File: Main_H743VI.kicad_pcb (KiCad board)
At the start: 4 copper layers, 150 x 100 mm, 71 parts, among them J1 ST-LINK, J10 AS7265X, J11 TFT_LCD2, J12 SERVO1, J13 USER_GPIO, J14 TFT_LCD, J15 SERVO2, J16 FAN, J17 ADC_IN, J2 USB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

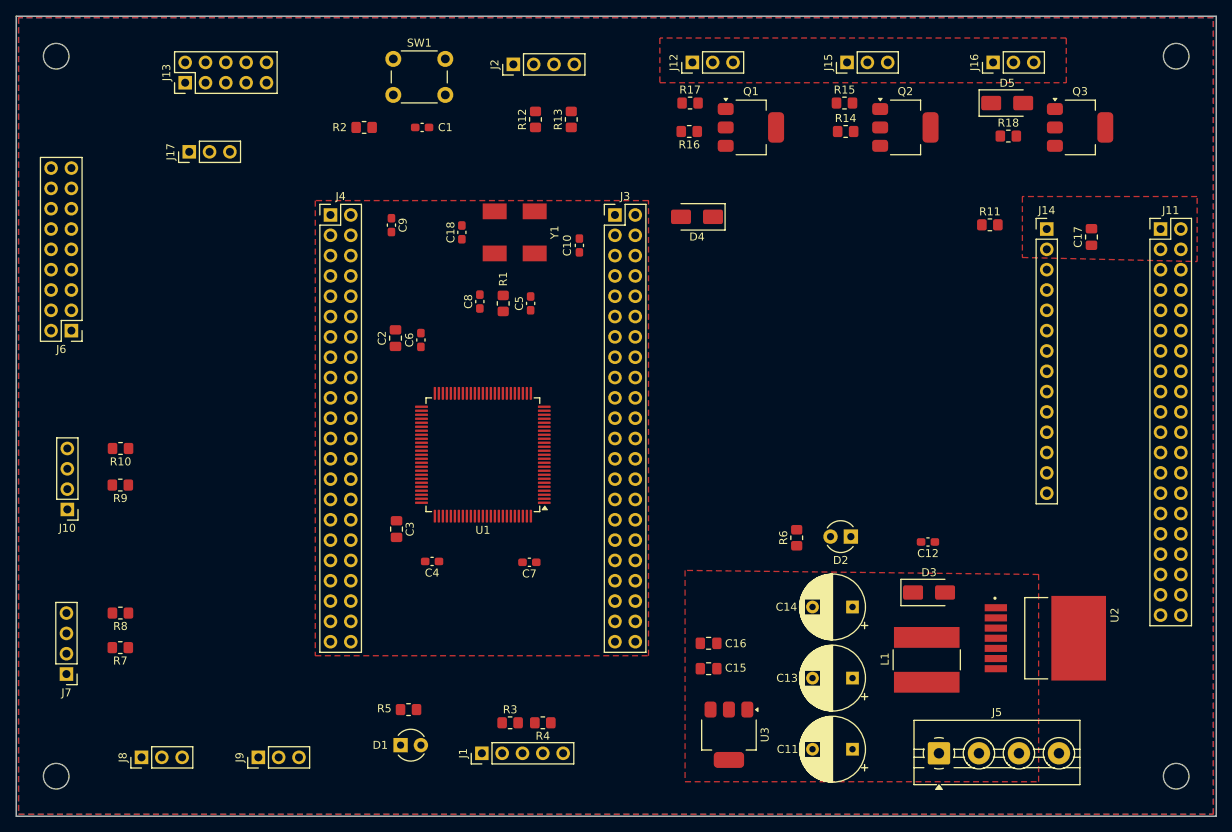
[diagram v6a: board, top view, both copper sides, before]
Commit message: flipped camera connector
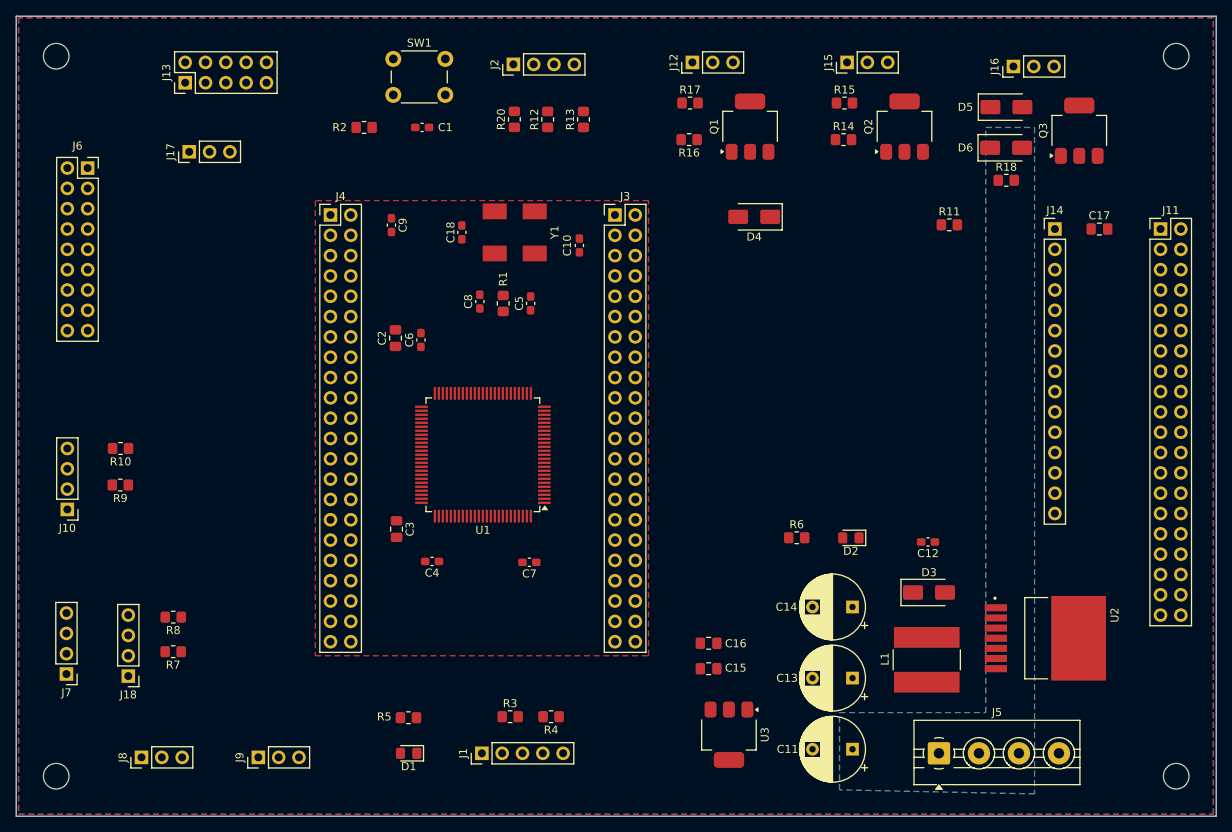
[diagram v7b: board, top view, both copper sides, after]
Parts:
- added D6: SS36, Diode_SMD:D_SMA, F.Cu at (198.7, 36.4)
- added J18: BME280, Connector_PinHeader_2.54mm:PinHeader_1x04_P2.54mm_Vertical, F.Cu at (89.0, 102.5)
- added R20: 0, Resistor_SMD:R_0805_2012Metric_Pad1.20x1.40mm_HandSolder, F.Cu at (137.3, 32.9)
- D1, D2: footprint LED_THT:LED_D3.0mm -> LED_SMD:LED_0805_2012Metric_Pad1.15x1.40mm_HandSolder
- J11: value TFT_LCD2 -> TFT_FMC
- J14: value TFT_LCD -> TFT_SPI; footprint Connector_PinHeader_2.54mm:PinHeader_1x14_P2.54mm_Vertical -> Connector_PinHeader_2.54mm:PinHeader_1x15_P2.54mm_Vertical
- J5: value Screw_Terminal_01x04 -> POWER
- J6: footprint Connector_PinHeader_2.54mm:PinHeader_2x09_P2.54mm_Vertical -> Connector_PinSocket_2.54mm:PinSocket_2x09_P2.54mm_Vertical
- moved J6 20.4 mm to (83.9, 39.0), turned to 0 degrees
- moved D4 7.14 mm to (167.2, 45.1)
- moved R7 6.62 mm to (94.6, 99.4)
- moved R8 6.62 mm to (94.6, 95.1)
- moved R18 5.53 mm to (198.8, 40.5)
- moved R11 5.06 mm to (191.6, 46.1)
- moved J16 2.59 mm to (199.7, 26.3)
- moved R12 1.52 mm to (141.4, 32.9)
- moved R13 1.52 mm to (145.9, 32.9)
- moved D1 1.43 mm to (124.1, 112.1), turned to 180 degrees
- moved C17 1.41 mm to (210.4, 46.6), turned to 0 degrees
- moved R4 1.28 mm to (141.9, 107.6)
- moved R14 1.05 mm to (178.4, 35.4)
- moved R16 1.02 mm to (159.1, 35.4)
- moved R5 1.02 mm to (124.0, 107.7)
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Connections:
- net Net-(J5-Pin_3) renamed +12V
- J2 pad 1: unconnected-(J2-Pin_1-Pad1) -> Net-(J2-Pin_1)
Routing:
- added copper zone on B.Cu, net +12V
- added copper zone on In2.Cu, net +3.3V
- added copper zone on F.Cu, net +5V
- added copper zone on In1.Cu, net GND
- removed copper zone on F.Cu, net +3.3V
- removed copper zone on F.Cu, net GND

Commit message: snapshot
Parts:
- added R19: 10K, Resistor_SMD:R_0805_2012Metric_Pad1.20x1.40mm_HandSolder, F.Cu at (132.2, 107.6)
- H1, H2, H3, H4: value MountingHole -> ~; footprint MountingHole:MountingHole_3.2mm_M3 -> PCM_JLCPCB:Hole, 3mm
- L1: footprint Inductor_SMD:L_Bourns-SRN8040_8x8.15mm -> JLCPCB:L_SMD,8x8mm
- Q1, Q2, Q3: footprint Package_TO_SOT_SMD:SOT-223-3_TabPin2 -> PCM_Package_TO_SOT_SMD_AKL:SOT-223-3_TabPin2
- moved C15 5.15 mm to (165.2, 97.9)
- moved C16 4.77 mm to (165.2, 101.5)
- moved D2 1.64 mm to (179.9, 86.7)
- moved R6 1.64 mm to (173.2, 86.7)
- moved C12 1.02 mm to (189.0, 86.7)
- moved Q2 0.71 mm to (186.0, 34.5)
- moved Q1 0.61 mm to (166.7, 34.4)
- moved R3 0.51 mm to (137.2, 107.6)
- moved R4 0.51 mm to (142.4, 107.6)
- moved Q3 0.20 mm to (207.9, 34.5)
